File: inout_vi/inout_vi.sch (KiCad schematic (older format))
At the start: 1 part, among them P1 DIN_41612_128P

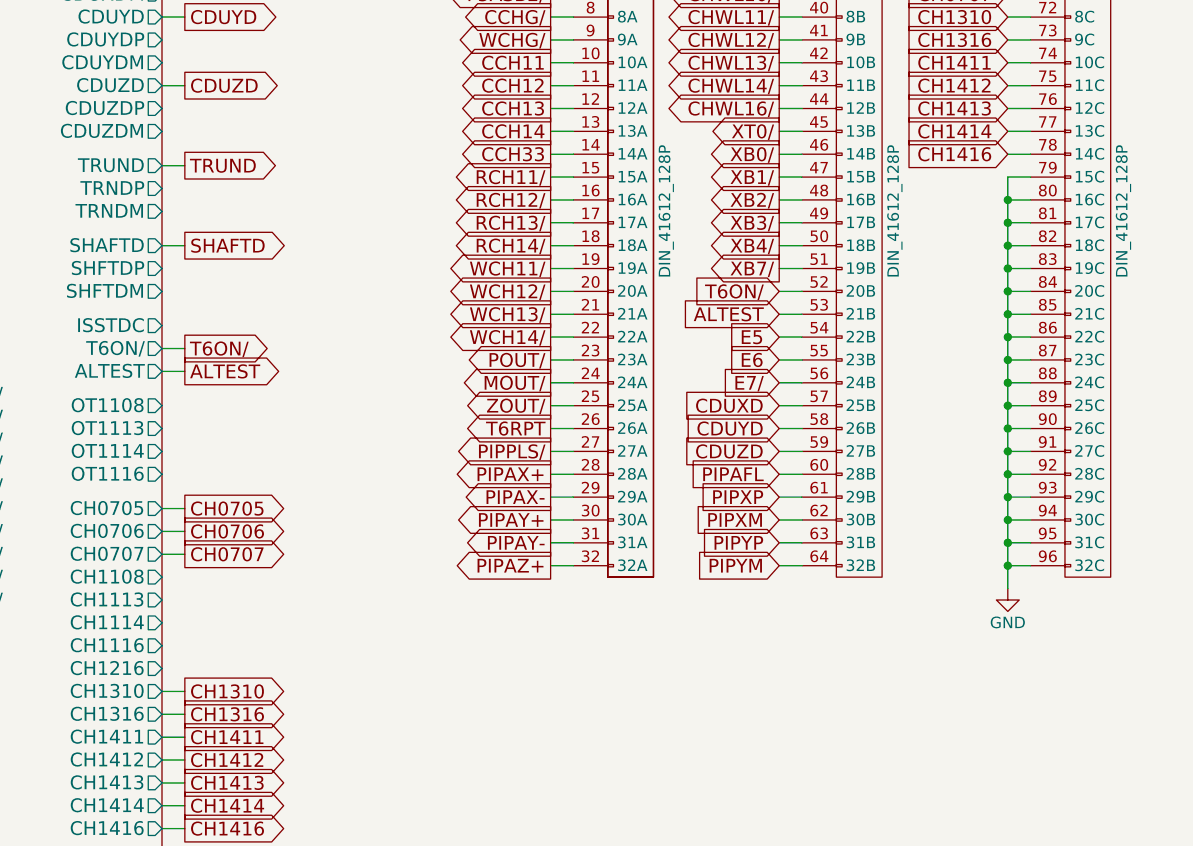
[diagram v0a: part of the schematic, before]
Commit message: Added and tied in Inout VII, the final logic module!
I still need to comb through the schematics to see if there are any
stray gates I missed. The initial conditions are also pretty much
guaranteed to be wrong. But it's mostly all there!
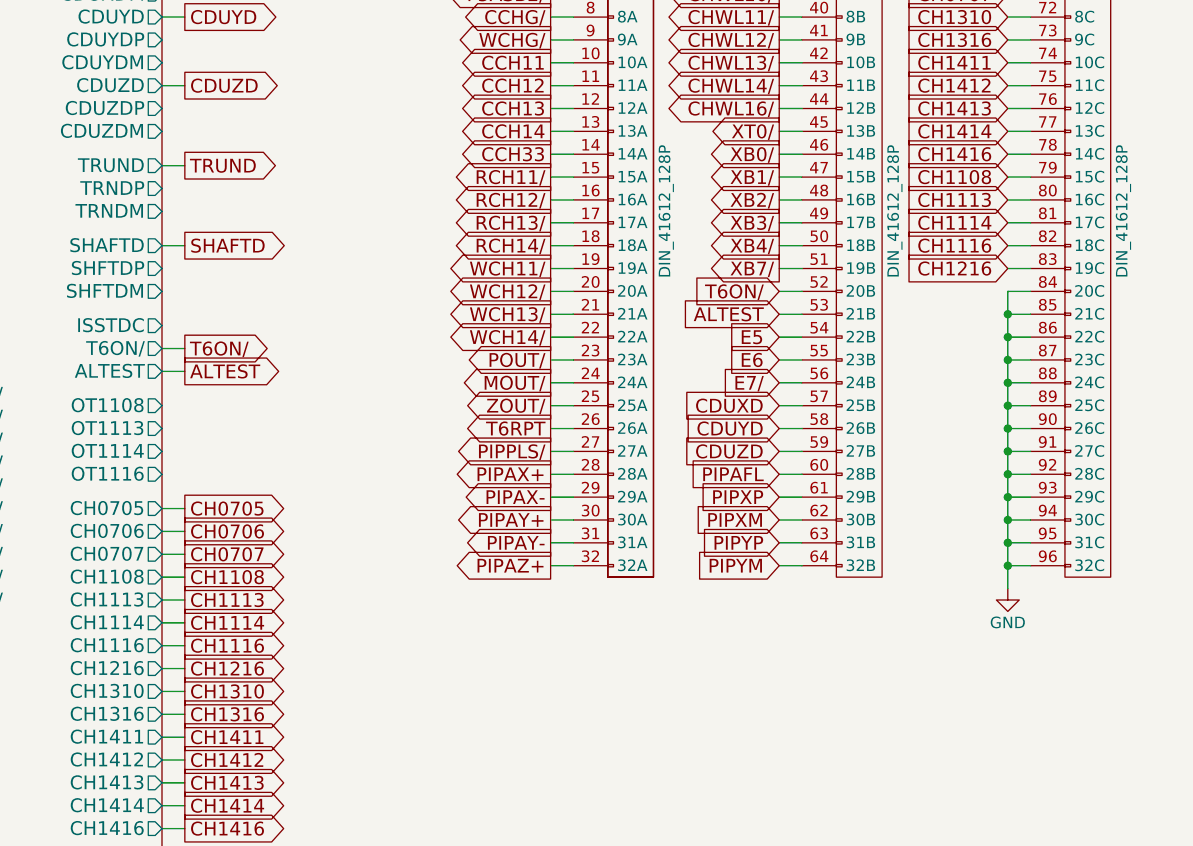
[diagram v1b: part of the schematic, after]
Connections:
- net GND: no longer P1.79 (15C), P1.80 (16C), P1.81 (17C), P1.82 (18C), P1.83 (19C)
- new net CH1108: P1.79 (15C)
- new net CH1113: P1.80 (16C)
- new net CH1114: P1.81 (17C)
- new net CH1116: P1.82 (18C)
- new net CH1216: P1.83 (19C)
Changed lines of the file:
@@
 $EndComp
 Wire Wire Line
-	8450 2850 8550 2850
-Wire Wire Line
-	8450 2950 8550 2950
-Connection ~ 8450 2950
-Wire Wire Line
-	8450 3050 8550 3050
-Connection ~ 8450 3050
-Wire Wire Line
-	8450 3150 8550 3150
-Connection ~ 8450 3150
-Wire Wire Line
-	8450 3250 8550 3250
-Connection ~ 8450 3250
-Wire Wire Line
 	8450 3350 8550 3350
-Connection ~ 8450 3350
 Wire Wire Line
 	8450 3450 8550 3450
@@
 Text GLabel 4850 3600 2    60   Output ~ 0
 T6ON/
-Wire Wire Line
-	8450 2850 8450 4650
 Text GLabel 7450 3350 0    60   Input ~ 0
 T6ON/
 Wire Wire Line
 	7450 3350 7550 3350
+Wire Wire Line
+	4750 4600 4850 4600
+Text GLabel 4850 4600 2    60   Output ~ 0
+CH1108
+Wire Wire Line
+	4750 4700 4850 4700
+Text GLabel 4850 4700 2    60   Output ~ 0
+CH1113
+Wire Wire Line
+	4750 4800 4850 4800
+Text GLabel 4850 4800 2    60   Output ~ 0
+CH1114
+Wire Wire Line
+	4750 4900 4850 4900
+Text GLabel 4850 4900 2    60   Output ~ 0
+CH1116
+Wire Wire Line
+	4750 5000 4850 5000
+Text GLabel 4850 5000 2    60   Output ~ 0
+CH1216
+Wire Wire Line
+	8550 2950 8450 2950
+Text GLabel 8450 2950 0    60   Input ~ 0
+CH1113
+Wire Wire Line
+	8550 3050 8450 3050
+Text GLabel 8450 3050 0    60   Input ~ 0
+CH1114
+Wire Wire Line
+	8550 3150 8450 3150
+Text GLabel 8450 3150 0    60   Input ~ 0
+CH1116
+Wire Wire Line
+	8550 3250 8450 3250
+Text GLabel 8450 3250 0    60   Input ~ 0
+CH1216
+Wire Wire Line
+	8550 2850 8450 2850
+Text GLabel 8450 2850 0    60   Input ~ 0
+CH1108
+Wire Wire Line
+	8450 3350 8450 4650
 $EndSCHEMATC

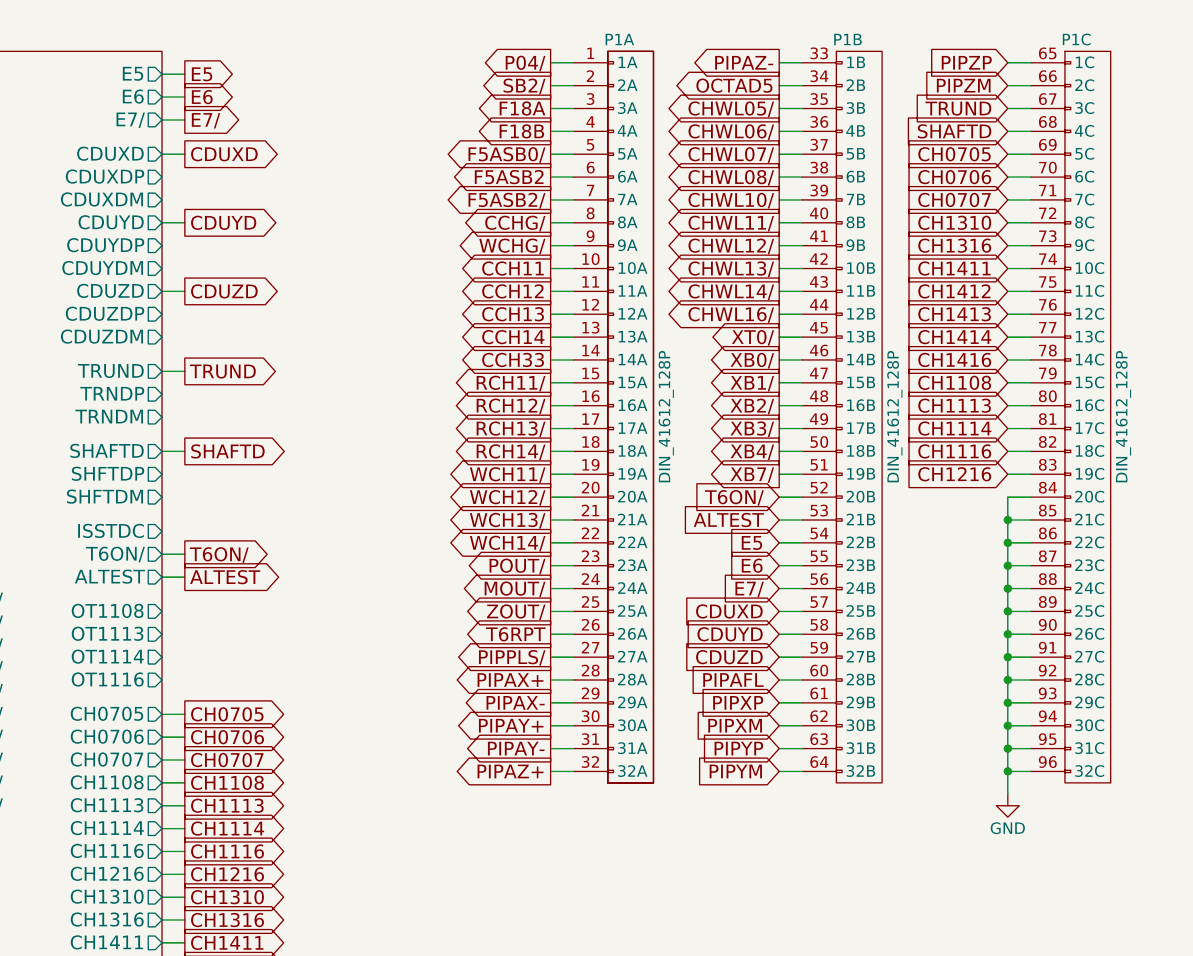
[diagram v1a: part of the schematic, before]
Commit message: Broke out some PIPA and CDU-related output signals, and fixed the polarity of PIPPLS/
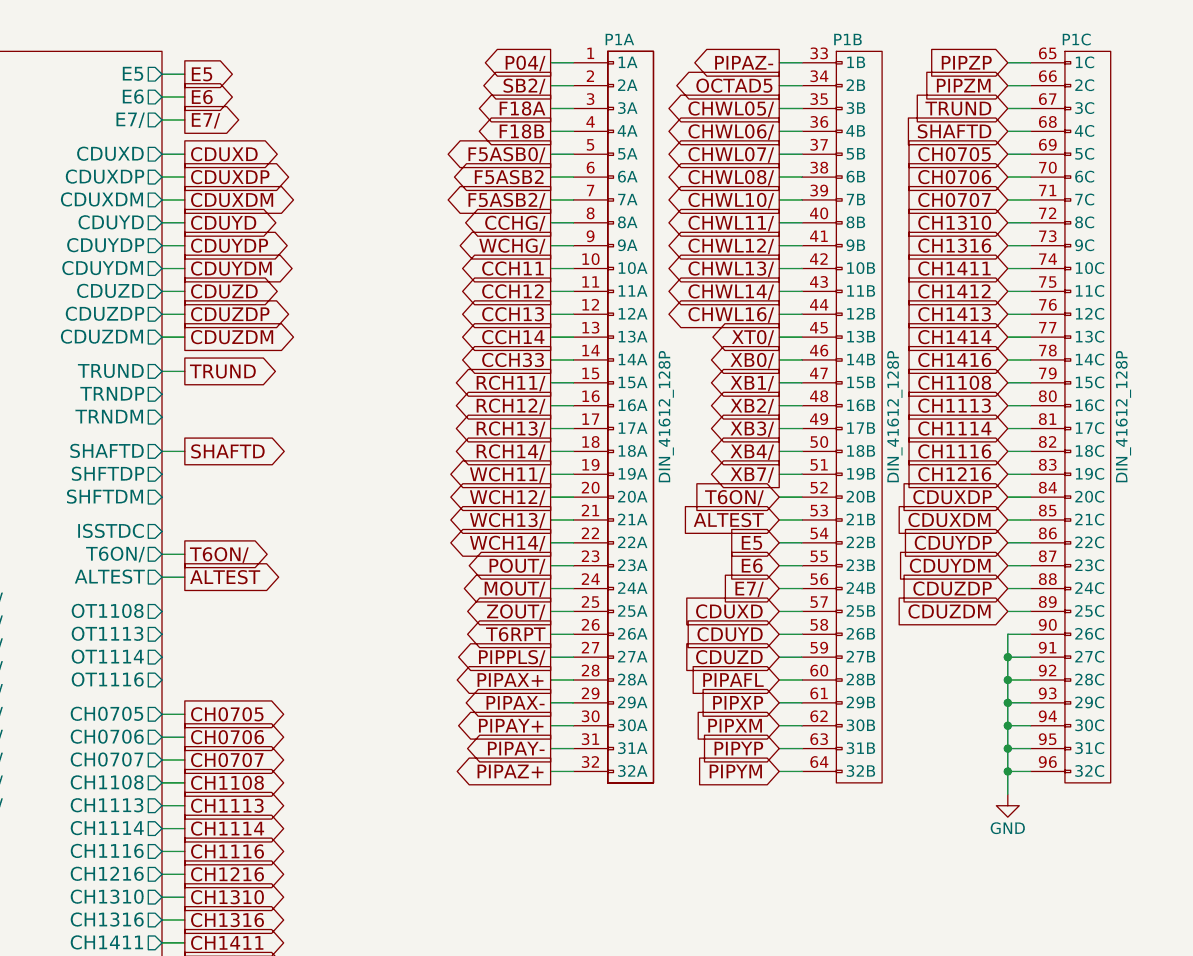
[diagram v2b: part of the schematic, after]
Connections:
- net GND: no longer P1.84 (20C), P1.85 (21C), P1.86 (22C), P1.87 (23C), P1.88 (24C), P1.89 (25C)
- new net CDUXDM: P1.85 (21C)
- new net CDUXDP: P1.84 (20C)
- new net CDUYDM: P1.87 (23C)
- new net CDUYDP: P1.86 (22C)
- new net CDUZDM: P1.89 (25C)
- new net CDUZDP: P1.88 (24C)
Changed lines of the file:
@@
 $EndComp
 Wire Wire Line
-	8450 3350 8550 3350
-Wire Wire Line
-	8450 3450 8550 3450
-Connection ~ 8450 3450
-Wire Wire Line
-	8450 3550 8550 3550
-Connection ~ 8450 3550
-Wire Wire Line
-	8450 3650 8550 3650
-Connection ~ 8450 3650
-Wire Wire Line
-	8450 3750 8550 3750
-Connection ~ 8450 3750
-Wire Wire Line
-	8450 3850 8550 3850
-Connection ~ 8450 3850
-Wire Wire Line
 	8450 3950 8550 3950
-Connection ~ 8450 3950
 Wire Wire Line
 	8450 4050 8550 4050
@@
 CH1108
 Wire Wire Line
-	8450 3350 8450 4650
+	4750 1950 4850 1950
+Text GLabel 4850 1950 2    60   Output ~ 0
+CDUXDP
+Wire Wire Line
+	4750 2050 4850 2050
+Text GLabel 4850 2050 2    60   Output ~ 0
+CDUXDM
+Wire Wire Line
+	4750 2250 4850 2250
+Text GLabel 4850 2250 2    60   Output ~ 0
+CDUYDP
+Wire Wire Line
+	4750 2350 4850 2350
+Text GLabel 4850 2350 2    60   Output ~ 0
+CDUYDM
+Wire Wire Line
+	4750 2550 4850 2550
+Text GLabel 4850 2550 2    60   Output ~ 0
+CDUZDP
+Wire Wire Line
+	4750 2650 4850 2650
+Text GLabel 4850 2650 2    60   Output ~ 0
+CDUZDM
+Wire Wire Line
+	8450 4650 8450 3950
+Wire Wire Line
+	8550 3350 8450 3350
+Text GLabel 8450 3350 0    60   Input ~ 0
+CDUXDP
+Wire Wire Line
+	8550 3450 8450 3450
+Text GLabel 8450 3450 0    60   Input ~ 0
+CDUXDM
+Wire Wire Line
+	8550 3550 8450 3550
+Text GLabel 8450 3550 0    60   Input ~ 0
+CDUYDP
+Wire Wire Line
+	8550 3650 8450 3650
+Text GLabel 8450 3650 0    60   Input ~ 0
+CDUYDM
+Wire Wire Line
+	8550 3750 8450 3750
+Text GLabel 8450 3750 0    60   Input ~ 0
+CDUZDP
+Wire Wire Line
+	8550 3850 8450 3850
+Text GLabel 8450 3850 0    60   Input ~ 0
+CDUZDM
 $EndSCHEMATC

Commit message: Updated Inout VI to be on +4VSW
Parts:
- added U23001, U23005, U23006, U23009, U23010, U23013, U23014, U23015, U23017, U23022, U23023, U23024, U23026, U23030, U23037, U23046: 74HC27, symbol 74HC27
- added U23002: 74LVC07, symbol 74LVC07
- added U23003, U23018, U23032, U23047, U23053, U23056: 74HC04, symbol 74HC04
- added U23004, U23007, U23008, U23011, U23012, U23016, U23019, U23020, U23021, U23025, U23027, U23028, U23029, U23031, U23033, U23034, U23035, U23036, U23038, U23039, U23040, U23041, U23042, U23043, U23044, U23045, U23048, U23049, U23050, U23051, U23052, U23054, U23055, U23057, U23058: 74HC02, symbol 74HC02
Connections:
- net labels added: +4VSW
- net labels removed: VCC
- wire segments 286 -> 297
